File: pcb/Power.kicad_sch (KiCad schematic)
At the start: 3 parts, among them U4 LD39050PU33R

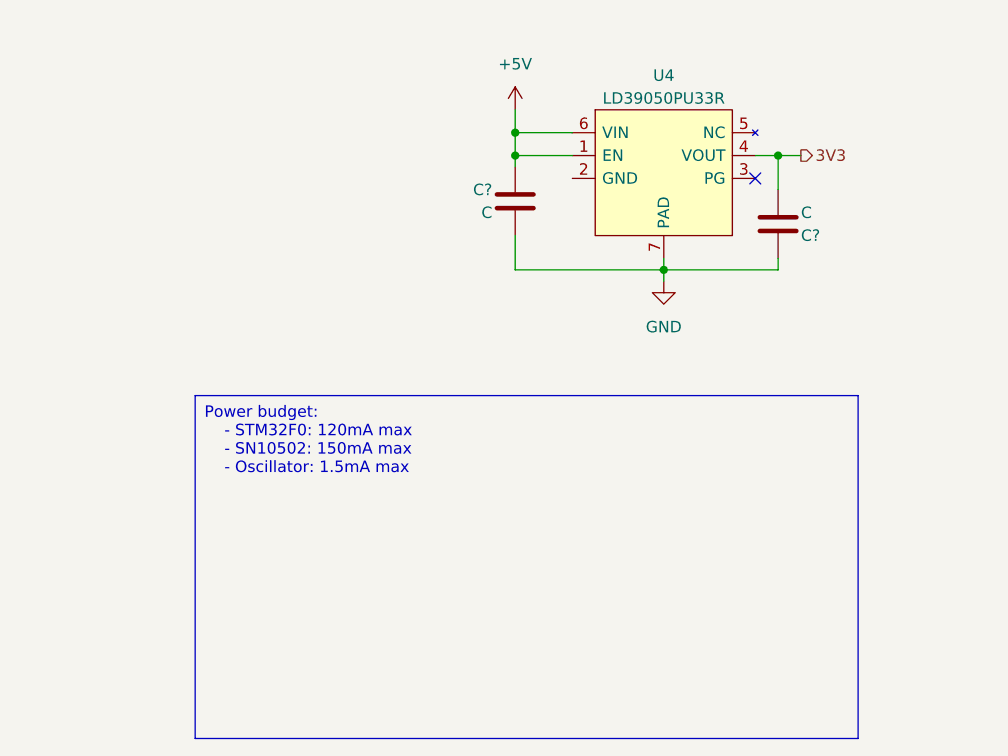
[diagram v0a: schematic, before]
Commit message: Completed schematic oranization and components connection
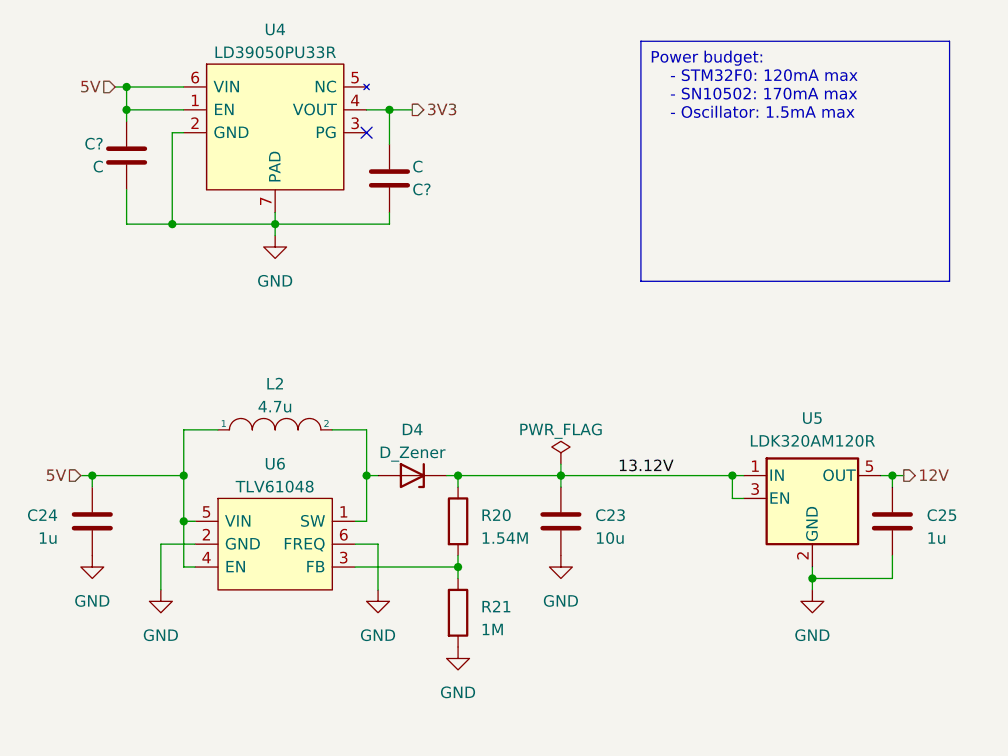
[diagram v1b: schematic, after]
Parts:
- added C23: 10u, symbol Device:C
- added C24, C25: 1u, symbol Device:C
- added D4: D_Zener, symbol Device:D_Zener
- added L2: 4.7u, symbol pspice:INDUCTOR
- added R20: 1.54M, symbol Device:R
- added R21: 1M, symbol Device:R
- added U5: LDK320AM120R, symbol Signal Generator Components:LDK320AM120R
- added U6: TLV61048, Skyward library:TLV61048, symbol Signal Generator Components:TLV61048
- U4: footprint Signal Generator Components:LD39050PU33R -> Skyward library:LD39050PU33R
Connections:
- net GND: now also U4.2 (GND), C23.2, C24.2, C25.2, R21.2, U5.2 (GND), U6.2 (GND), U6.6 (FREQ)
- net +5V renamed 5V
- net 5V: now also C24.1, L2.1, U6.4 (EN), U6.5 (VIN)
- new net: R20.2, R21.1, U6.3 (FB)
- new net: D4.2 (A), L2.2, U6.1 (SW)
- new net 12V: C25.1, U5.5 (OUT)
- new net 13.12V: C23.1, D4.1 (K), R20.1, U5.1 (IN), U5.3 (EN)
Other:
- moved on the sheet: C?, U4

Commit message: Added micro SD and RGB led to schematic. Also added components part numbers
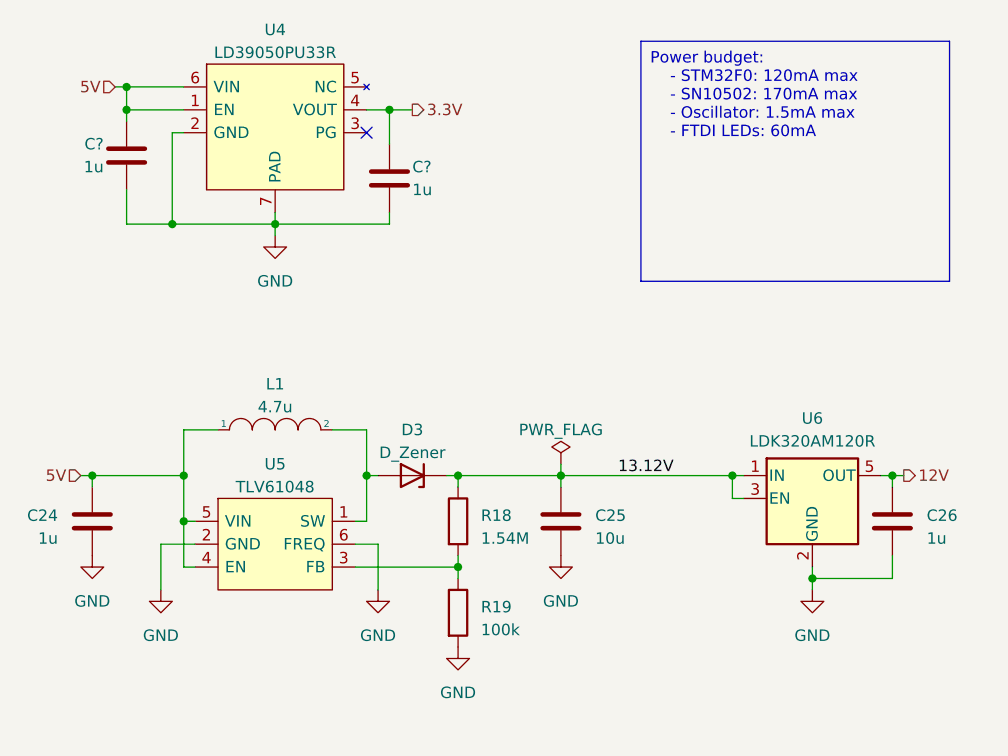
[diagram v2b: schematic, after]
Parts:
- C24: footprint (none) -> Capacitor_SMD:C_0603_1608Metric; PN (none) -> GCM188R71C105KA64D
- C25: renamed from C23; footprint (none) -> Capacitor_SMD:C_0603_1608Metric; PN (none) -> GRM188D71A106KA73D
- C26: renamed from C25; footprint (none) -> Capacitor_SMD:C_0603_1608Metric; PN (none) -> GCM188R71C105KA64D
- C? (x2): value C -> 1u; PN (none) -> GCM188R71C105KA64D
- D3: renamed from D4; footprint (none) -> Signal Generator Components:BZT52C10-TP; PN (none) -> BZT52C10-TP
- L1: renamed from L2; footprint (none) -> Signal Generator Components:XAL4030; PN (none) -> XAL4030-472MEC
- R18: renamed from R20; footprint (none) -> Capacitor_SMD:C_0603_1608Metric; PN (none) -> RC0603FR-071M54L
- R19: renamed from R21; value 1M -> 100k; footprint (none) -> Capacitor_SMD:C_0603_1608Metric; PN (none) -> ERJ-3EKF1003V
- U4: footprint Skyward library:LD39050PU33R -> Signal Generator Components:LD39050PU33R; PN (none) -> LD39050PU33R
- U5: renamed from U6; footprint Skyward library:TLV61048 -> Signal Generator Components:TLV61048; PN (none) -> TLV61048DBVR
- U6: renamed from U5; footprint (none) -> Signal Generator Components:LDK320AM120R; PN (none) -> LDK320AM120R
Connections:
- net GND: now also C?.2; no longer C?.1
- net 3V3 renamed 3.3V
- net 3.3V: now also C?.1; no longer C?.2

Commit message: Completed schematic and tried some simulations
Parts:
- renumbered D3 to D4, R18 to R19, R19 to R20
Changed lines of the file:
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@@
   (title_block
     (title "Power")
+    (date "2023-01-16")
+    (rev "0")
   )
   (junction (at 143.51 116.84) (diameter 0) (color 0 0 0 0)
@@
   (symbol (lib_id "Device:R") (at 143.51 121.92 0) (unit 1)
     (in_bom yes) (on_board yes) (dnp no) (fields_autoplaced)
-    (property "Reference" "R18" (at 146.05 121.285 0)
+    (property "Reference" "R19" (at 146.05 121.285 0)
       (effects (font (size 1.27 1.27)) (justify left))
     )
@@
       (project "Signal Generator"
         (path "/f6255c48-6253-4c69-a6db-1ceaf4eff04d/755a5482-c972-48ba-877b-a349f74d45fc"
-          (reference "R18") (unit 1)
+          (reference "R19") (unit 1)
         )
       )
@@
   (symbol (lib_id "Device:R") (at 143.51 132.08 0) (unit 1)
     (in_bom yes) (on_board yes) (dnp no) (fields_autoplaced)
-    (property "Reference" "R19" (at 146.05 131.445 0)
+    (property "Reference" "R20" (at 146.05 131.445 0)
       (effects (font (size 1.27 1.27)) (justify left))
     )
@@
       (project "Signal Generator"
         (path "/f6255c48-6253-4c69-a6db-1ceaf4eff04d/755a5482-c972-48ba-877b-a349f74d45fc"
-          (reference "R19") (unit 1)
+          (reference "R20") (unit 1)
         )
       )
@@
   (symbol (lib_id "Device:D_Zener") (at 138.43 116.84 180) (unit 1)
     (in_bom yes) (on_board yes) (dnp no) (fields_autoplaced)
-    (property "Reference" "D3" (at 138.43 111.76 0)
+    (property "Reference" "D4" (at 138.43 111.76 0)
       (effects (font (size 1.27 1.27)))
     )
@@
       (project "Signal Generator"
         (path "/f6255c48-6253-4c69-a6db-1ceaf4eff04d/755a5482-c972-48ba-877b-a349f74d45fc"
-          (reference "D3") (unit 1)
-        )
-      )
+          (reference "D4") (unit 1)
+        )
+      )

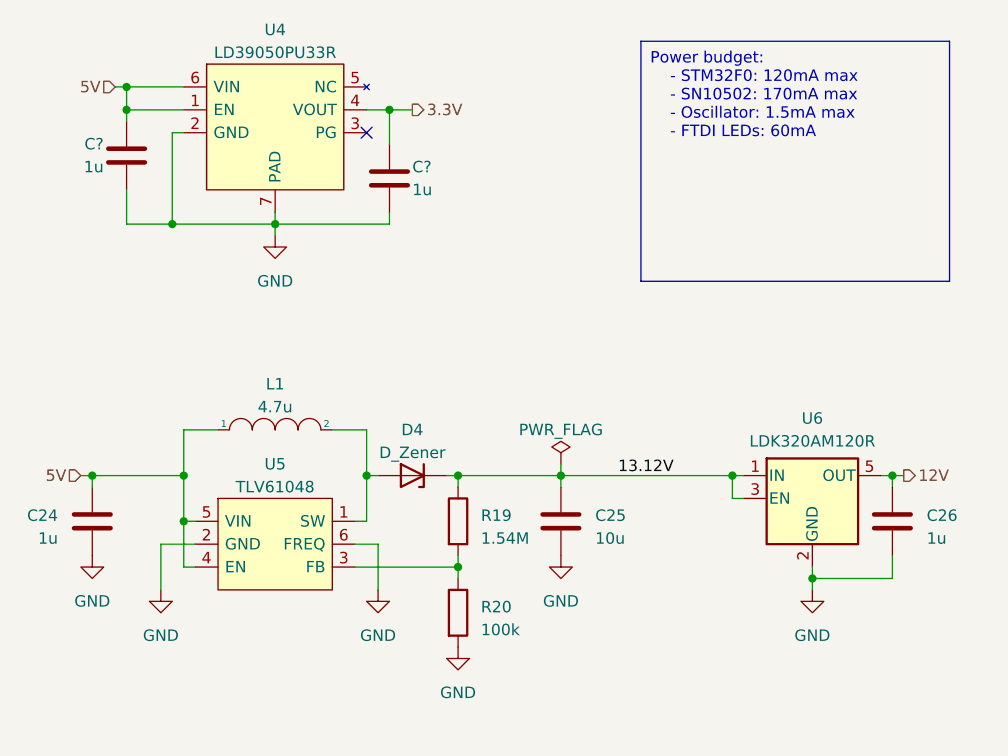
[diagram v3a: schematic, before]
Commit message: Added blocking capacitor to headphones jack
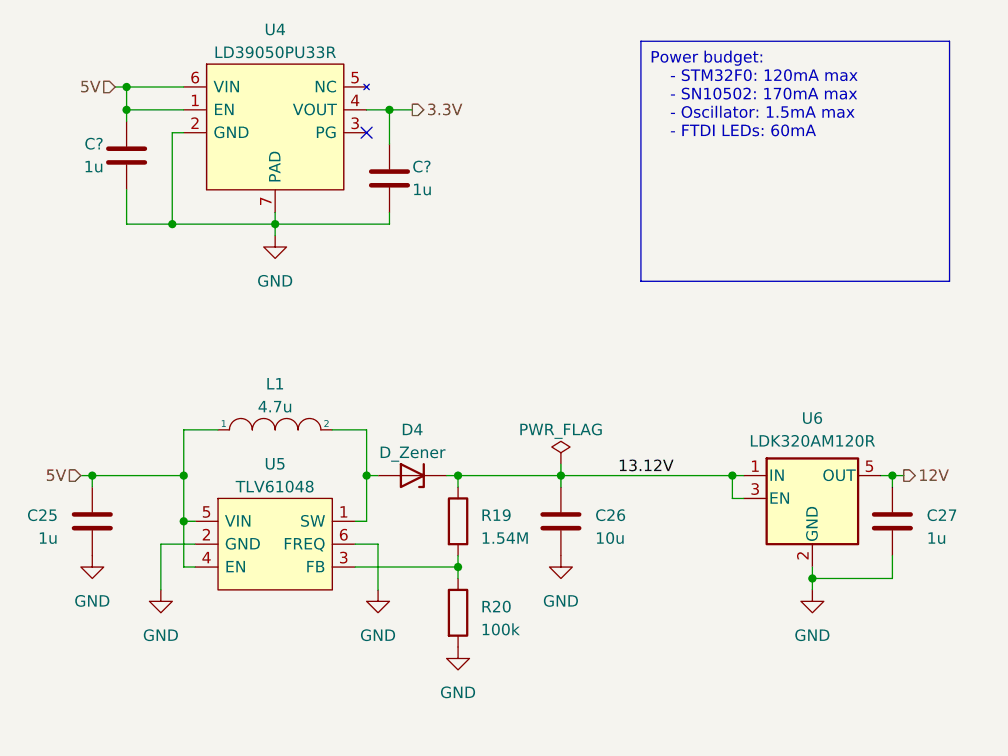
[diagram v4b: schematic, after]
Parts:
- renumbered C24 to C25, C25 to C26, C26 to C27
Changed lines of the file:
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@@
         )
         (path "/f6255c48-6253-4c69-a6db-1ceaf4eff04d/755a5482-c972-48ba-877b-a349f74d45fc"
-          (reference "C23") (unit 1)
+          (reference "C24") (unit 1)
         )
       )
@@
   (symbol (lib_id "Device:C") (at 191.77 121.92 0) (unit 1)
     (in_bom yes) (on_board yes) (dnp no) (fields_autoplaced)
-    (property "Reference" "C26" (at 195.58 121.285 0)
+    (property "Reference" "C27" (at 195.58 121.285 0)
       (effects (font (size 1.27 1.27)) (justify left))
     )
@@
       (project "Signal Generator"
         (path "/f6255c48-6253-4c69-a6db-1ceaf4eff04d/755a5482-c972-48ba-877b-a349f74d45fc"
+          (reference "C27") (unit 1)
+        )
+      )
+    )
+  )
+  (symbol (lib_id "Device:C") (at 154.94 121.92 0) (unit 1)
+    (in_bom yes) (on_board yes) (dnp no) (fields_autoplaced)
+    (property "Reference" "C26" (at 158.75 121.285 0)
+      (effects (font (size 1.27 1.27)) (justify left))
+    )
+    (property "Value" "10u" (at 158.75 123.825 0)
+      (effects (font (size 1.27 1.27)) (justify left))
+    )
+    (property "Footprint" "Capacitor_SMD:C_0603_1608Metric" (at 155.9052 125.73 0)
+      (effects (font (size 1.27 1.27)) hide)
+    )
+    (property "Datasheet" "~" (at 154.94 121.92 0)
+      (effects (font (size 1.27 1.27)) hide)
+    )
+    (property "PN" "GRM188D71A106KA73D" (at 154.94 121.92 0)
+      (effects (font (size 1.27 1.27)) hide)
+    )
+    (pin "1")
+    (pin "2")
+    (instances
+      (project "Signal Generator"
+        (path "/f6255c48-6253-4c69-a6db-1ceaf4eff04d/755a5482-c972-48ba-877b-a349f74d45fc"
           (reference "C26") (unit 1)
-        )
-      )
-    )
-  )
-  (symbol (lib_id "Device:C") (at 154.94 121.92 0) (unit 1)
-    (in_bom yes) (on_board yes) (dnp no) (fields_autoplaced)
-    (property "Reference" "C25" (at 158.75 121.285 0)
-      (effects (font (size 1.27 1.27)) (justify left))
-    )
-    (property "Value" "10u" (at 158.75 123.825 0)
-      (effects (font (size 1.27 1.27)) (justify left))
-    )
-    (property "Footprint" "Capacitor_SMD:C_0603_1608Metric" (at 155.9052 125.73 0)
-      (effects (font (size 1.27 1.27)) hide)
-    )
-    (property "Datasheet" "~" (at 154.94 121.92 0)
-      (effects (font (size 1.27 1.27)) hide)
-    )
-    (property "PN" "GRM188D71A106KA73D" (at 154.94 121.92 0)
-      (effects (font (size 1.27 1.27)) hide)
-    )
-    (pin "1")
-    (pin "2")
-    (instances
-      (project "Signal Generator"
-        (path "/f6255c48-6253-4c69-a6db-1ceaf4eff04d/755a5482-c972-48ba-877b-a349f74d45fc"
-          (reference "C25") (unit 1)
         )
       )
@@
   (symbol (lib_id "Device:C") (at 102.87 121.92 0) (mirror y) (unit 1)
     (in_bom yes) (on_board yes) (dnp no)
-    (property "Reference" "C24" (at 99.06 121.285 0)
+    (property "Reference" "C25" (at 99.06 121.285 0)
       (effects (font (size 1.27 1.27)) (justify left))
     )
@@
       (project "Signal Generator"
         (path "/f6255c48-6253-4c69-a6db-1ceaf4eff04d/755a5482-c972-48ba-877b-a349f74d45fc"
-          (reference "C24") (unit 1)
+          (reference "C25") (unit 1)
         )
       )
@@
         )
         (path "/f6255c48-6253-4c69-a6db-1ceaf4eff04d/755a5482-c972-48ba-877b-a349f74d45fc"
-          (reference "C22") (unit 1)
-        )
-      )
+          (reference "C23") (unit 1)
+        )
+      )
